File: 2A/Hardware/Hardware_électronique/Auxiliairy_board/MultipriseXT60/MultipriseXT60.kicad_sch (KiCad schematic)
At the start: 11 parts, among them J1 Conn_01x02_Pin, J2 Conn_01x02_Pin, J3 Conn_01x02_Pin, J4 Conn_01x02_Pin, J5 Conn_01x02_Pin, J6 Conn_01x02_Pin

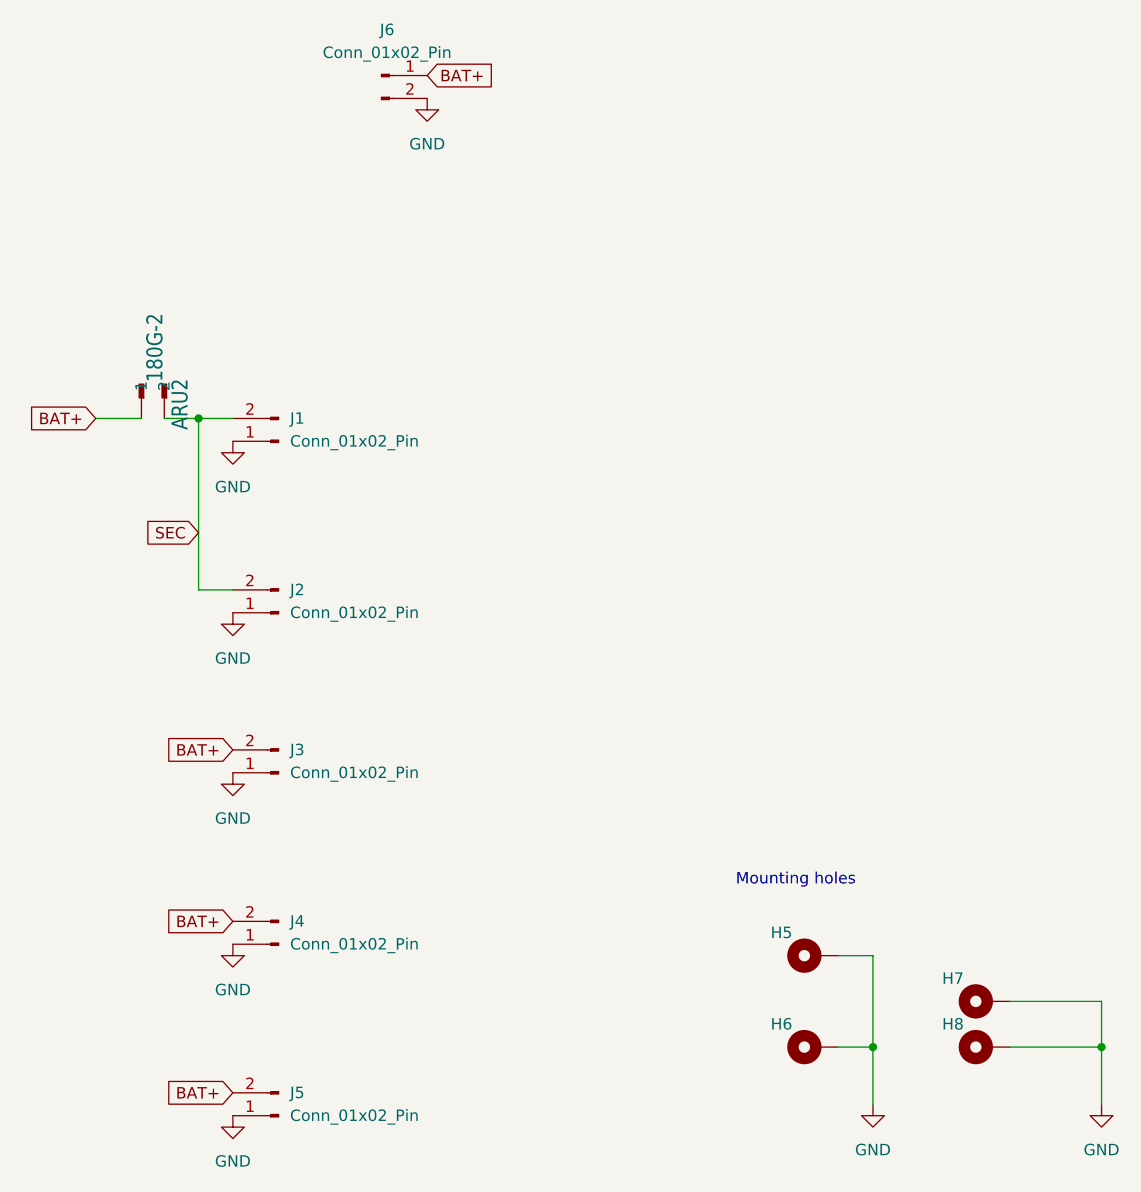
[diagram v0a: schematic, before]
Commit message: change on kicad projects, remove errors
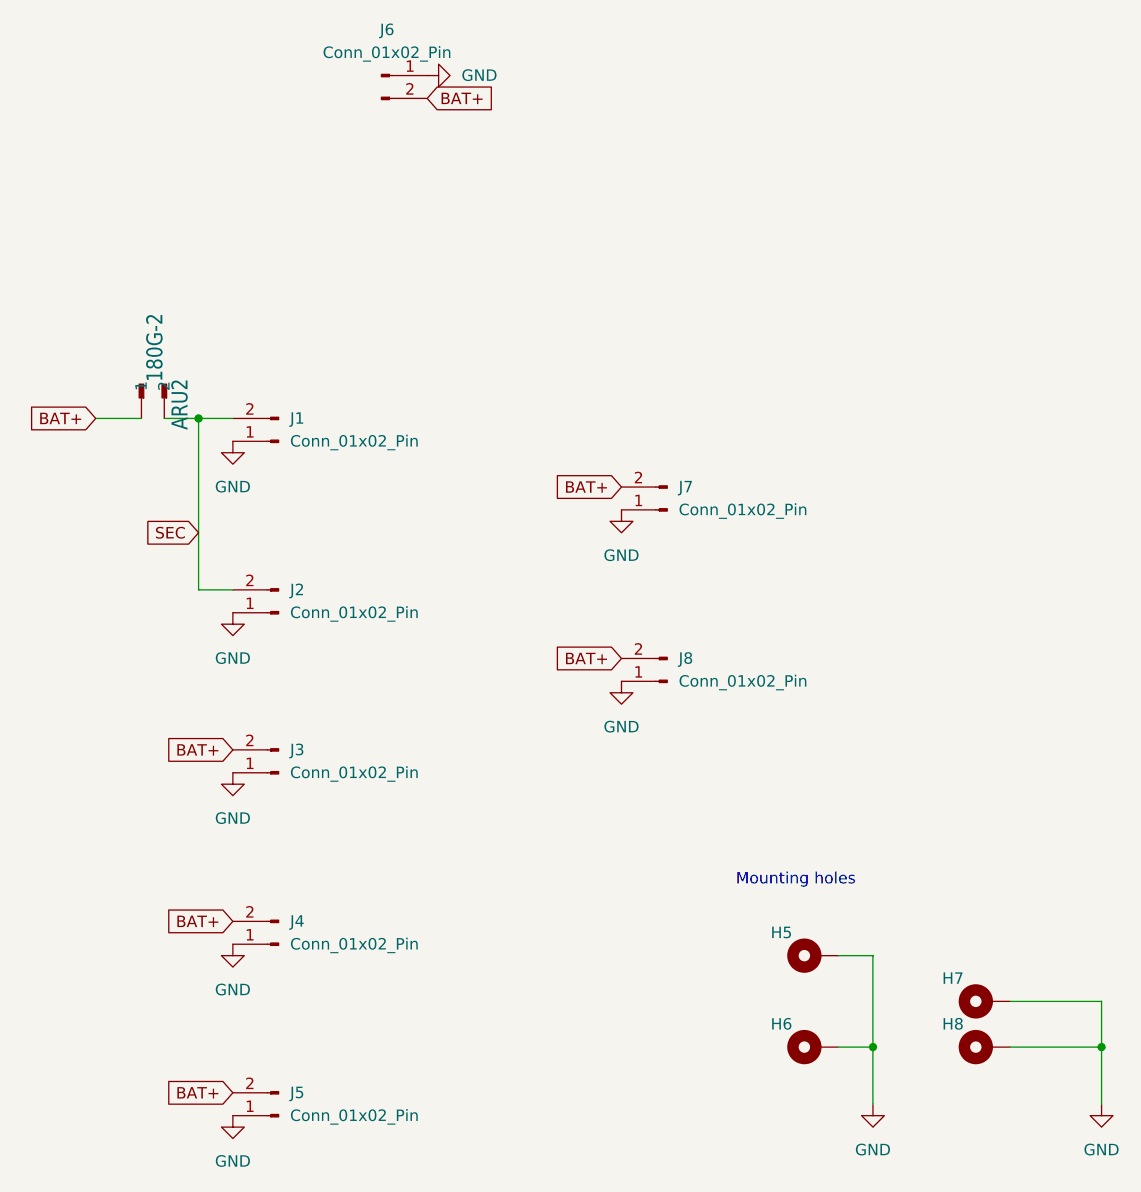
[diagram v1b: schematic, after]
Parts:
- added J7, J8: Conn_01x02_Pin, Connector_AMASS:AMASS_XT60-F_1x02_P7.20mm_Vertical, symbol Connector:Conn_01x02_Pin
- ARU2: footprint Button_Switch_THT:SW_CW_GPTS203211B -> Connector_AMASS:AMASS_XT60-F_1x02_P7.20mm_Vertical
- J1, J2, J3, J4, J5, J6: footprint Connector_AMASS:AMASS_XT60PW-F_1x02_P7.20mm_Horizontal -> Connector_AMASS:AMASS_XT60-F_1x02_P7.20mm_Vertical
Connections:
- net BAT+: now also J6.2 (Pin_2), J7.2 (Pin_2), J8.2 (Pin_2); no longer J6.1 (Pin_1)
- net GND: now also J6.1 (Pin_1), J7.1 (Pin_1), J8.1 (Pin_1); no longer J6.2 (Pin_2)
